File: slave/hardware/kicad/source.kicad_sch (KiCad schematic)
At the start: 47 parts, among them IC1 L6982C50, IC2 L6982C33, IC3 STEF12SGR, IC4 STEF12SGR, Q1 IPD50P04P4L-11

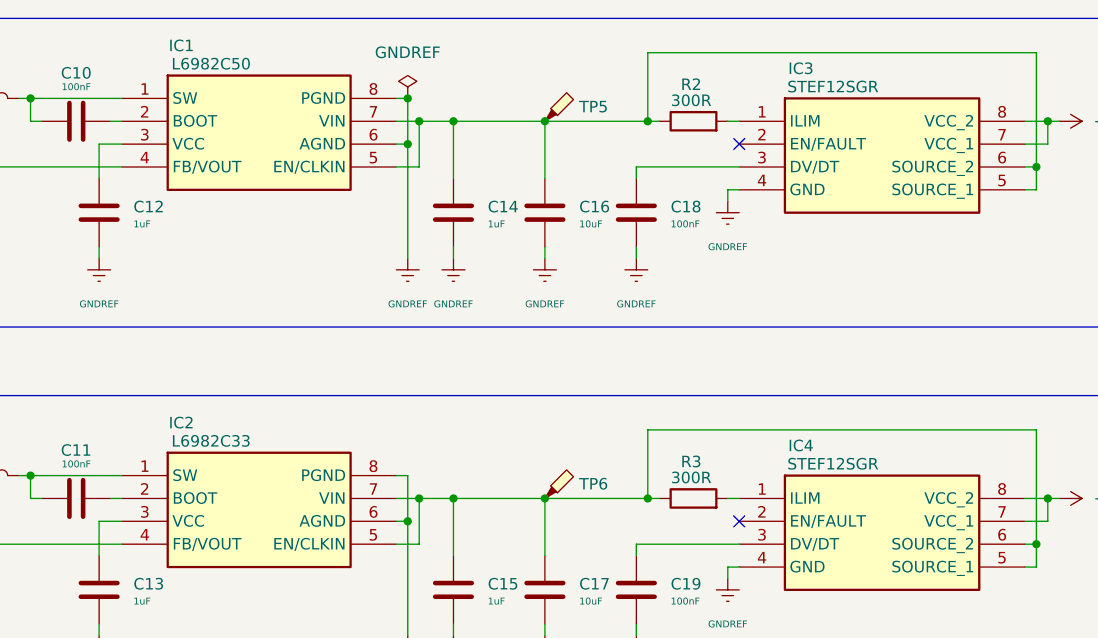
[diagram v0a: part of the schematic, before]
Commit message: fix(HW): resolve KiCad ERC warnings
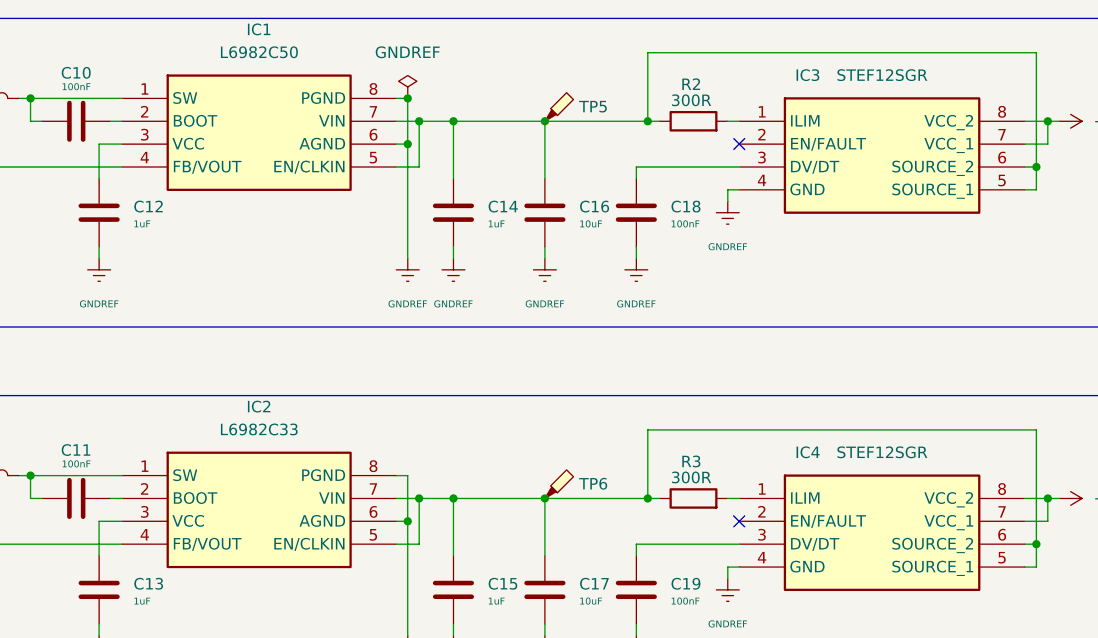
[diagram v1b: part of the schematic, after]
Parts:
- removed IC1: L6982C50, Datalogger:SOIC127P600X175-8N, symbol Datalogger Slave:L6982CDR
- removed IC2: L6982C33, Datalogger:SOIC127P600X175-8N, symbol Datalogger Slave:L6982CDR
- removed IC3, IC4: STEF12SGR, Datalogger:SOIC127P600X175-8N, symbol Datalogger Slave:STEF12SGR
- added IC1: L6982C50, Datalogger:SOIC127P600X175-8N, symbol Datalogger:L6982CDR
- added IC2: L6982C33, Datalogger:SOIC127P600X175-8N, symbol Datalogger:L6982CDR
- added IC3, IC4: STEF12SGR, Datalogger:SOP65P280X100-8N, symbol Datalogger:STEF12SGR
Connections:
- net +12V: now also IC3.7 (VCC_1), IC3.8 (VCC_2), IC4.7 (VCC_1), IC4.8 (VCC_2)
- net +3.3V: now also IC2.4 (FB/VOUT)
- net +5V: now also IC1.4 (FB/VOUT)
- net GNDREF: now also IC1.6 (AGND), IC1.8 (PGND), IC2.6 (AGND), IC2.8 (PGND), IC3.4 (GND), IC4.4 (GND)
- net at C11.2, L2.2: now also IC2.1 (SW)
- net at R2.2: now also IC3.1 (ILIM)
- net at C18.1: now also IC3.3 (DV/DT)
- net at C14.1, C16.1, R2.1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: now also IC1.5 (EN/CLKIN), IC1.7 (VIN), IC3.5 (SOURCE_1), IC3.6 (SOURCE_2)
- net at C15.1, C17.1, R3.1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: now also IC2.5 (EN/CLKIN), IC2.7 (VIN), IC4.5 (SOURCE_1), IC4.6 (SOURCE_2)
- net at C10.2, L1.2: now also IC1.1 (SW)
- net at C10.1: now also IC1.2 (BOOT)
- net at C12.1: now also IC1.3 (VCC)
- net at R3.2: now also IC4.1 (ILIM)
- net at C11.1: now also IC2.2 (BOOT)
- net at C13.1: now also IC2.3 (VCC)
- net at C19.1: now also IC4.3 (DV/DT)

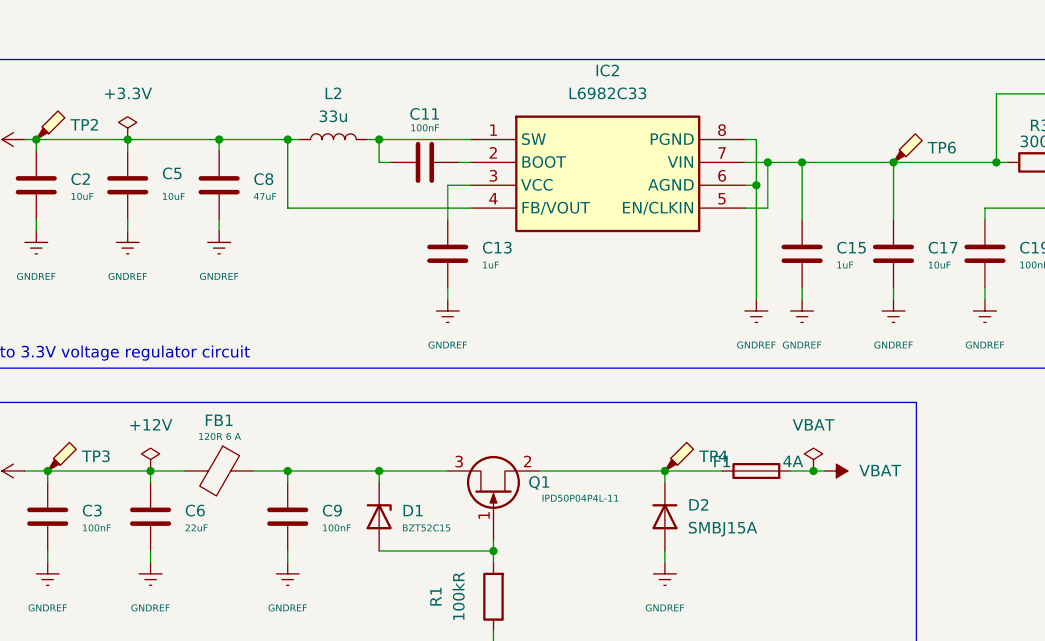
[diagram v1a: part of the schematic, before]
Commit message: feat(HW): continue PCB layout and routing updates
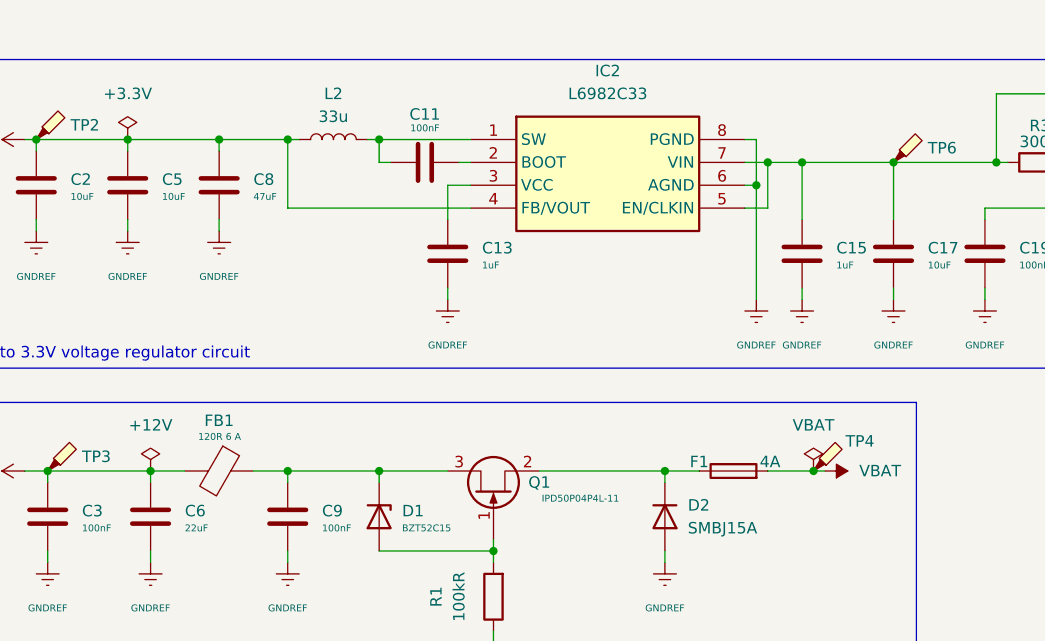
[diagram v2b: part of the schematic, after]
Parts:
- C1, C10, C11, C12, C13, C14, C15, C16, C17, C18, C19, C2, C3, C4, C5, C6, C7, C8, C9: footprint Capacitor_SMD:C_0201_0603Metric -> Capacitor_SMD:C_0603_1608Metric
- D3, D4, D5, D6: footprint LED_SMD:LED_01005_0402Metric -> LED_SMD:LED_0805_2012Metric
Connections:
- net VBAT: now also TP4.1
- net at D2.1 (K), F1.1, Q1.2 (S): no longer TP4.1
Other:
- moved on the sheet: F1, TP4
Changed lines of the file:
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@@
 	)
 	(junction
-		(at 156.21 130.81)
-		(diameter 0)
-		(color 255 243 0 1)
-	)
-	(junction
 		(at 219.71 101.6)
 		(diameter 0)
@@
 		(color 0 0 0 1)
 	)
+	(junction
+		(at 156.21 130.81)
+		(diameter 0)
+		(color 255 243 0 1)
+	)
 	(no_connect
 		(at 186.69 99.06)
@@
 	(wire
 		(pts
-			(xy 139.7 130.81) (xy 146.05 130.81)
+			(xy 139.7 130.81) (xy 143.51 130.81)
 		)
 		(stroke
@@
 	(wire
 		(pts
-			(xy 153.67 130.81) (xy 156.21 130.81)
+			(xy 151.13 130.81) (xy 156.21 130.81)
 		)
 		(stroke
@@
 			)
 		)
-		(property "Footprint" "Capacitor_SMD:C_0201_0603Metric"
+		(property "Footprint" "Capacitor_SMD:C_0603_1608Metric"
 			(at 83.5152 139.7 0)
 			(hide yes)
@@
 			)
 		)
-		(property "Footprint" "Capacitor_SMD:C_0201_0603Metric"
+		(property "Footprint" "Capacitor_SMD:C_0603_1608Metric"
 			(at 70.8152 60.96 0)
 			(hide yes)
@@
 			)
 		)
-		(property "Footprint" "Capacitor_SMD:C_0201_0603Metric"
+		(property "Footprint" "Capacitor_SMD:C_0603_1608Metric"
 			(at 91.1352 60.96 0)
 			(hide yes)
@@
 			)
 		)
-		(property "Footprint" "LED_SMD:LED_01005_0402Metric"
+		(property "Footprint" "LED_SMD:LED_0805_2012Metric"
 			(at 207.01 144.78 0)
 			(hide yes)
@@
 			)
 		)
-		(property "Footprint" "Capacitor_SMD:C_0201_0603Metric"
+		(property "Footprint" "Capacitor_SMD:C_0603_1608Metric"
 			(at 166.0652 68.58 0)
 			(hide yes)
@@
 			)
 		)
-		(property "Footprint" "Capacitor_SMD:C_0201_0603Metric"
+		(property "Footprint" "Capacitor_SMD:C_0603_1608Metric"
 			(at 176.2252 68.58 0)
 			(hide yes)
@@
 			)
 		)
-		(property "Footprint" "Capacitor_SMD:C_0201_0603Metric"
+		(property "Footprint" "Capacitor_SMD:C_0603_1608Metric"
 			(at 72.0852 139.7 0)
 			(hide yes)
@@
 			)
 		)
-		(property "Footprint" "Capacitor_SMD:C_0201_0603Metric"
+		(property "Footprint" "Capacitor_SMD:C_0603_1608Metric"
 			(at 80.9752 60.96 0)
 			(hide yes)
@@
 			)
 		)
-		(property "Footprint" "LED_SMD:LED_01005_0402Metric"
+		(property "Footprint" "LED_SMD:LED_0805_2012Metric"
 			(at 224.79 144.78 0)
 			(hide yes)
@@
 			)
 		)
-		(property "Footprint" "Capacitor_SMD:C_0201_0603Metric"
+		(property "Footprint" "Capacitor_SMD:C_0603_1608Metric"
 			(at 109.22 97.4852 0)
 			(hide yes)
@@
 	(symbol
 		(lib_id "Connector:TestPoint_Probe")
-		(at 139.7 130.81 0)
+		(at 156.21 130.81 0)
 		(unit 1)
 		(body_style 1)
@@
 		(in_pos_files yes)
 		(dnp no)
-		(fields_autoplaced yes)
 		(property "Reference" "TP4"
-			(at 143.51 129.2224 0)
+			(at 159.766 127.508 0)
 			(show_name no)
 			(do_not_autoplace no)
@@
 		)
 		(property "Value" ""
-			(at 143.51 130.4924 0)
+			(at 160.02 130.4924 0)
 			(show_name no)
 			(do_not_autoplace no)
@@
 		)
 		(property "Footprint" "TestPoint:TestPoint_Pad_2.0x2.0mm"
-			(at 144.78 130.81 0)
+			(at 161.29 130.81 0)
 			(hide yes)
 			(show_name no)
@@
 		)
 		(property "Datasheet" ""
-			(at 144.78 130.81 0)
+			(at 161.29 130.81 0)
 			(hide yes)
 			(show_name no)
@@
 		)
 		(property "Description" "test point (alternative probe-style design)"
-			(at 139.7 130.81 0)
+			(at 156.21 130.81 0)
 			(hide yes)
 			(show_name no)
@@
 			)
 		)
-		(property "Footprint" "Capacitor_SMD:C_0201_0603Metric"
+		(property "Footprint" "Capacitor_SMD:C_0603_1608Metric"
 			(at 116.5352 110.49 0)
 			(hide yes)
@@
 			)
 		)
-		(property "Footprint" "Capacitor_SMD:C_0201_0603Metric"
+		(property "Footprint" "Capacitor_SMD:C_0603_1608Metric"
 			(at 70.8152 102.87 0)
 			(hide yes)
@@
 	(symbol
 		(lib_id "Device:Fuse")
-		(at 149.86 130.81 90)
+		(at 147.32 130.81 90)
 		(unit 1)
 		(body_style 1)
@@
 		(dnp no)
 		(property "Reference" "F1"
-			(at 146.05 129.794 90)
+			(at 143.51 129.794 90)
 			(show_name no)
 			(do_not_autoplace no)
@@
 		)
 		(property "Value" "4A"
-			(at 153.924 129.794 90)
+			(at 151.384 129.794 90)
 			(show_name no)
 			(do_not_autoplace no)
@@
 		)
 		(property "Footprint" "Fuse:Fuse_0805_2012Metric"
-			(at 149.86 132.588 90)
+			(at 147.32 132.588 90)
 			(hide yes)
 			(show_name no)
@@
 		)
 		(property "Datasheet" ""
-			(at 149.86 130.81 0)
+			(at 147.32 130.81 0)
 			(hide yes)
 			(show_name no)
@@
 		)
 		(property "Description" "Fuse"
-			(at 149.86 130.81 0)
+			(at 147.32 130.81 0)
 			(hide yes)
 			(show_name no)
@@
 			)
 		)
-		(property "Footprint" "Capacitor_SMD:C_0201_0603Metric"
+		(property "Footprint" "Capacitor_SMD:C_0603_1608Metric"
 			(at 109.22 55.5752 0)
 			(hide yes)
@@
 			)
 		)
-		(property "Footprint" "Capacitor_SMD:C_0201_0603Metric"
+		(property "Footprint" "Capacitor_SMD:C_0603_1608Metric"
 			(at 166.0652 110.49 0)
 			(hide yes)
@@
 			)
 		)
-		(property "Footprint" "Capacitor_SMD:C_0201_0603Metric"
+		(property "Footprint" "Capacitor_SMD:C_0603_1608Metric"
 			(at 155.9052 68.58 0)
 			(hide yes)
@@
 			)
 		)
-		(property "Footprint" "Capacitor_SMD:C_0201_0603Metric"
+		(property "Footprint" "Capacitor_SMD:C_0603_1608Metric"
 			(at 91.1352 102.87 0)
 			(hide yes)
@@
 			)
 		)
-		(property "Footprint" "LED_SMD:LED_01005_0402Metric"
+		(property "Footprint" "LED_SMD:LED_0805_2012Metric"
 			(at 215.9 144.78 0)
 			(hide yes)
@@
 			)
 		)
-		(property "Footprint" "Capacitor_SMD:C_0201_0603Metric"
+		(property "Footprint" "Capacitor_SMD:C_0603_1608Metric"
 			(at 98.7552 139.7 0)
 			(hide yes)
@@
 			)
 		)
-		(property "Footprint" "Capacitor_SMD:C_0201_0603Metric"
+		(property "Footprint" "Capacitor_SMD:C_0603_1608Metric"
 			(at 116.5352 68.58 0)
 			(hide yes)
@@
 		(fields_autoplaced yes)
 		(property "Reference" "C5"
-			(at 83.82 97.7899 0)
+			(at 83.82 98.4249 0)
 			(show_name no)
 			(do_not_autoplace no)
@@
 				(font
 					(size 1.27 1.27)
-					(color 255 106 0 1)
 				)
 				(justify left)
@@
 		)
 		(property "Value" "10uF"
-			(at 83.82 100.3299 0)
+			(at 83.82 100.33 0)
 			(show_name no)
 			(do_not_autoplace no)
@@
 			)
 		)
-		(property "Footprint" "Capacitor_SMD:C_0201_0603Metric"
+		(property "Footprint" "Capacitor_SMD:C_0603_1608Metric"
 			(at 80.9752 102.87 0)
 			(hide yes)
@@
 			)
 		)
-		(property "Footprint" "Capacitor_SMD:C_0201_0603Metric"
+		(property "Footprint" "Capacitor_SMD:C_0603_1608Metric"
 			(at 176.2252 110.49 0)
 			(hide yes)
@@
 			)
 		)
-		(property "Footprint" "Capacitor_SMD:C_0201_0603Metric"
+		(property "Footprint" "Capacitor_SMD:C_0603_1608Metric"
 			(at 155.9052 110.49 0)
 			(hide yes)
@@
 			)
 		)
-		(property "Footprint" "LED_SMD:LED_01005_0402Metric"
+		(property "Footprint" "LED_SMD:LED_0805_2012Metric"
 			(at 198.12 144.78 0)
 			(hide yes)
